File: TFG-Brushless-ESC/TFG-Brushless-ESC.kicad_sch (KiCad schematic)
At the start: 70 parts, among them J1 V, J2 USB C Receptacle, J3 HALL SENSORS, J4 SWD-I2C, J6 U, J7 W, J8 24V IN, SW1 BOOT0, SW2 NRST, U1 LM317L_SOT-89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

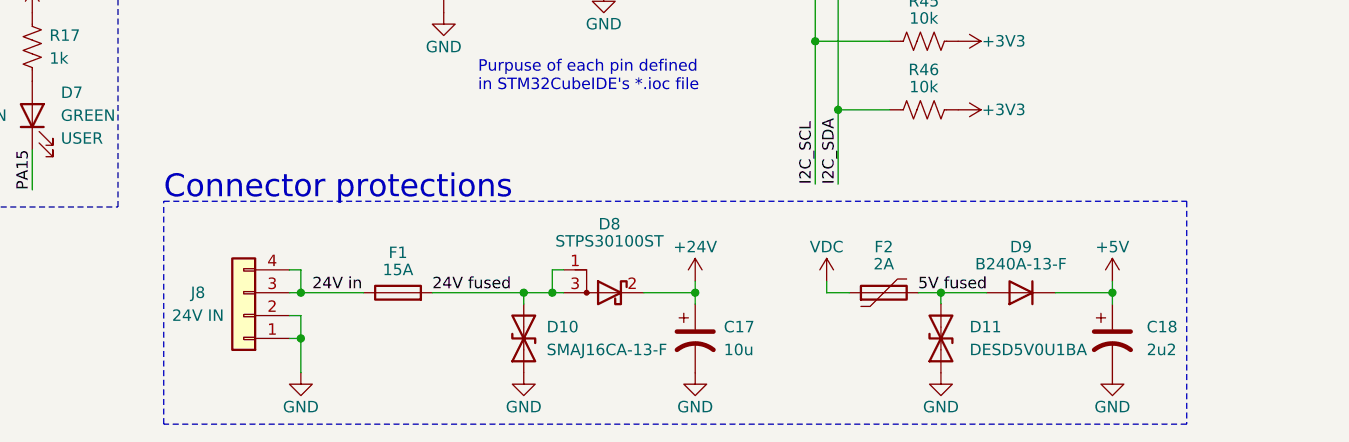
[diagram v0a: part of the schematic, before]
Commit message: renaming images
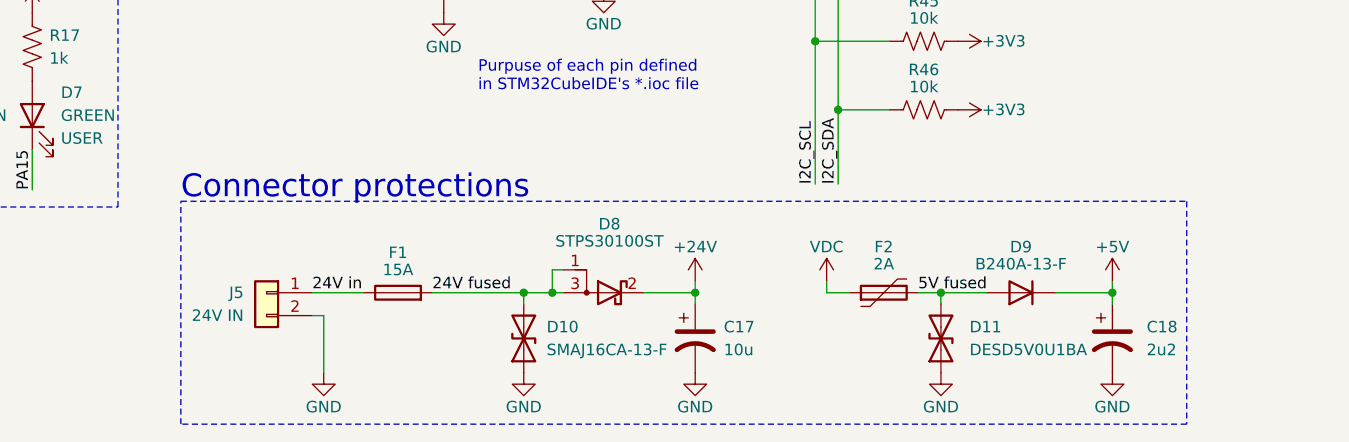
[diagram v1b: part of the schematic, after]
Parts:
- removed J8: 24V IN, Connector_Phoenix_MSTB:PhoenixContact_MSTBA_2,5_4-G-5,08_1x04_P5.08mm_Horizontal, symbol Connector_Generic:Conn_01x04
- added J5: 24V IN, Connector_Phoenix_MSTB:PhoenixContact_MSTBA_2,5_2-G-5,08_1x02_P5.08mm_Horizontal, symbol Connector_Generic:Conn_01x02
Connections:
- net 24V in: now also J5.1 (Pin_1)
- net GND: now also J5.2 (Pin_2)
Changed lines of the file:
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@@
 	)
 	(junction
-		(at 60.325 181.61)
-		(diameter 0)
-		(color 0 0 0 0)
-	)
-	(junction
 		(at 62.865 26.035)
 		(diameter 0)
@@
 	)
 	(junction
-		(at 60.325 186.69)
-		(diameter 0)
-		(color 0 0 0 0)
-	)
-	(junction
 		(at 34.29 122.555)
 		(diameter 0)
@@
 	(wire
 		(pts
-			(xy 60.325 186.69) (xy 60.325 190.5)
+			(xy 62.865 184.15) (xy 62.865 190.5)
 		)
 		(stroke
@@
 	(wire
 		(pts
-			(xy 59.055 184.15) (xy 60.325 184.15)
+			(xy 61.595 184.15) (xy 62.865 184.15)
 		)
 		(stroke
@@
 	(wire
 		(pts
-			(xy 60.325 186.69) (xy 60.325 184.15)
-		)
-		(stroke
-			(width 0)
-			(type default)
-		)
-	)
-	(wire
-		(pts
 			(xy 232.41 130.81) (xy 237.49 130.81)
 		)
@@
 	(wire
 		(pts
-			(xy 59.055 181.61) (xy 60.325 181.61)
+			(xy 61.595 181.61) (xy 67.31 181.61)
 		)
 		(stroke
@@
 	(wire
 		(pts
-			(xy 60.325 179.07) (xy 60.325 181.61)
-		)
-		(stroke
-			(width 0)
-			(type default)
-		)
-	)
-	(wire
-		(pts
 			(xy 237.49 130.81) (xy 237.49 136.525)
 		)
@@
 	(wire
 		(pts
-			(xy 59.055 186.69) (xy 60.325 186.69)
-		)
-		(stroke
-			(width 0)
-			(type default)
-		)
-	)
-	(wire
-		(pts
 			(xy 95.25 26.035) (xy 95.25 27.305)
 		)
@@
 	(wire
 		(pts
-			(xy 60.325 181.61) (xy 67.31 181.61)
-		)
-		(stroke
-			(width 0)
-			(type default)
-		)
-	)
-	(wire
-		(pts
 			(xy 164.465 36.195) (xy 164.465 33.655)
 		)
@@
 	(wire
 		(pts
-			(xy 59.055 179.07) (xy 60.325 179.07)
-		)
-		(stroke
-			(width 0)
-			(type default)
-		)
-	)
-	(wire
-		(pts
 			(xy 236.22 34.925) (xy 236.22 36.195)
 		)
@@
 	)
 	(rectangle
-		(start 45.085 171.45)
+		(start 46.99 171.45)
 		(end 158.75 196.215)
 		(stroke
@@
 	(text "Connector protections"
 		(exclude_from_sim no)
-		(at 45.085 171.45 0)
+		(at 46.99 171.45 0)
 		(effects
 			(font
@@
 	)
 	(symbol
-		(lib_id "Connector_Generic:Conn_01x04")
-		(at 53.975 184.15 180)
-		(unit 1)
-		(exclude_from_sim no)
-		(in_bom yes)
-		(on_board yes)
-		(dnp no)
-		(property "Reference" "J8"
-			(at 48.895 181.61 0)
-			(effects
-				(font
-					(size 1.27 1.27)
-				)
-			)
-		)
-		(property "Value" "24V IN"
-			(at 48.895 184.15 0)
-			(effects
-				(font
-					(size 1.27 1.27)
-				)
-			)
-		)
-		(property "Footprint" "Connector_Phoenix_MSTB:PhoenixContact_MSTBA_2,5_4-G-5,08_1x04_P5.08mm_Horizontal"
-			(at 53.975 184.15 0)
-			(effects
-				(font
-					(size 1.27 1.27)
-				)
-				(hide yes)
-			)
-		)
-		(property "Datasheet" "https://www.lcsc.com/datasheet/lcsc_datasheet_2408130957_Ningbo-Kangnex-Elec-WJ2EDGRC-5-08-4P_C8446.pdf"
-			(at 53.975 184.15 0)
-			(effects
-				(font
-					(size 1.27 1.27)
-				)
-				(hide yes)
-			)
-		)
-		(property "Description" "C8446"
-			(at 53.975 184.15 0)
-			(effects
-				(font
-					(size 1.27 1.27)
-				)
-				(hide yes)
-			)
-		)
-		(pin "1"
-		)
-		(pin "3"
-		)
-		(pin "2"
-		)
-		(pin "4"
-		)
-		(instances
-			(project ""
-				(path "/fc8dd9a9-f99a-4338-8182-2c8b4b8ed6dd"
-					(reference "J8")
-					(unit 1)
-				)
-			)
-		)
-	)
-	(symbol
 		(lib_id "Device:R_US")
 		(at 95.25 31.115 0)
@@
 	(symbol
 		(lib_id "power:GND")
-		(at 60.325 190.5 0)
+		(at 62.865 190.5 0)
 		(mirror y)
 		(unit 1)
@@
 		(dnp no)
 		(property "Reference" "#PWR054"
-			(at 60.325 196.85 0)
+			(at 62.865 196.85 0)
 			(effects
 				(font
@@
 		)
 		(property "Value" "GND"
-			(at 60.325 194.31 0)
+			(at 62.865 194.31 0)
 			(effects
 				(font
@@
 		)
 		(property "Footprint" ""
-			(at 60.325 190.5 0)
+			(at 62.865 190.5 0)
 			(effects
 				(font
@@
 		)
 		(property "Datasheet" ""
-			(at 60.325 190.5 0)
+			(at 62.865 190.5 0)
 			(effects
 				(font
@@
 		)
 		(property "Description" ""
-			(at 60.325 190.5 0)
+			(at 62.865 190.5 0)
 			(effects
 				(font
@@
 					(unit 1)
 				)
+			)
+		)
+	)
+	(symbol
+		(lib_id "Connector_Generic:Conn_01x02")
+		(at 56.515 181.61 0)
+		(mirror y)
+		(unit 1)
+		(exclude_from_sim no)
+		(in_bom yes)
+		(on_board yes)
+		(dnp no)
+		(property "Reference" "J5"
+			(at 53.975 181.61 0)
+			(effects
+				(font
+					(size 1.27 1.27)
+				)
+				(justify left)
+			)
+		)
+		(property "Value" "24V IN"
+			(at 53.975 184.15 0)
+			(effects
+				(font
+					(size 1.27 1.27)
+				)
+				(justify left)
+			)
+		)
+		(property "Footprint" "Connector_Phoenix_MSTB:PhoenixContact_MSTBA_2,5_2-G-5,08_1x02_P5.08mm_Horizontal"
+			(at 56.515 181.61 0)
+			(effects
+				(font
+					(size 1.27 1.27)
+				)
+				(hide yes)
+			)
+		)
+		(property "Datasheet" "https://www.lcsc.com/datasheet/lcsc_datasheet_2408130957_Ningbo-Kangnex-Elec-WJ2EDGRC-5-08-2P_C3697.pdf"
+			(at 56.515 181.61 0)
+			(effects
+				(font
+					(size 1.27 1.27)
+				)
+				(hide yes)
+			)
+		)
+		(property "Description" "C3697"
+			(at 56.515 181.61 0)
+			(effects
+				(font
+					(size 1.27 1.27)
+				)
+				(hide yes)
+			)
+		)
+		(pin "2"
+		)
+		(pin "1"
+		)
+		(instances
+			(project "TFG-Brushless-ESC"
+				(path "/fc8dd9a9-f99a-4338-8182-2c8b4b8ed6dd"
+					(reference "J5")
+					(unit 1)
+				)

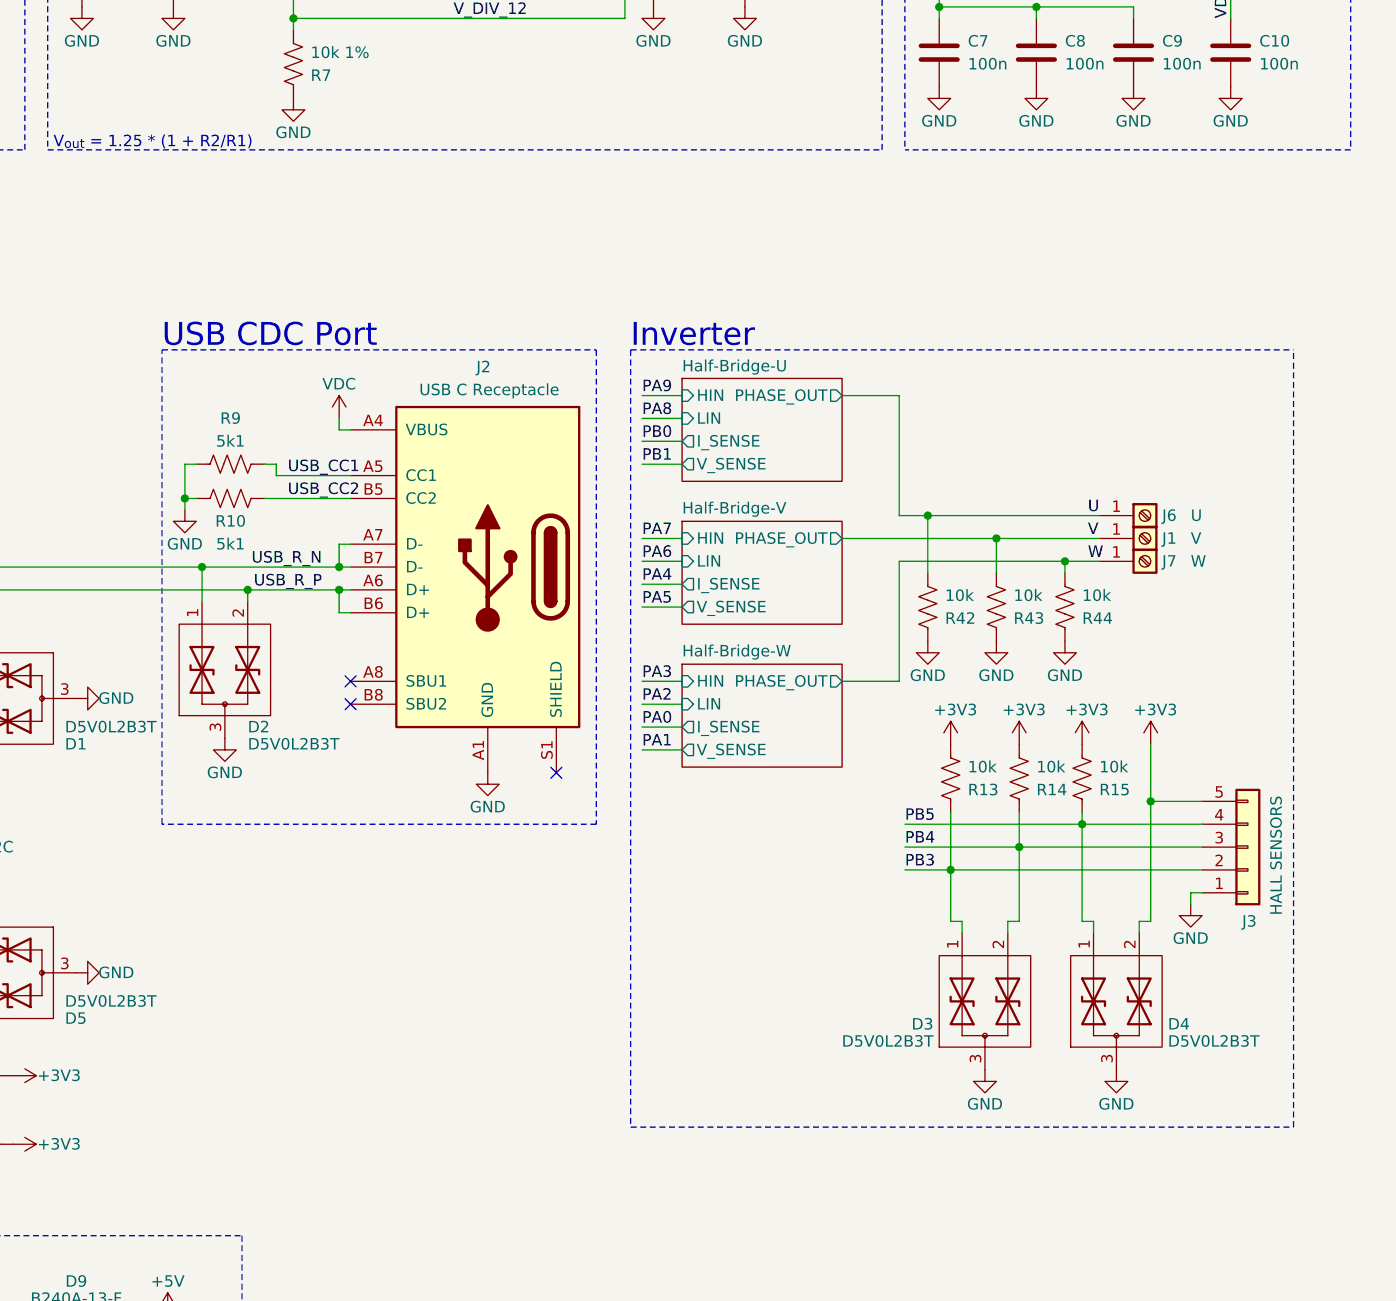
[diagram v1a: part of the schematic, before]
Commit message: Added fan control and temp measurement. Not added to pcb yet
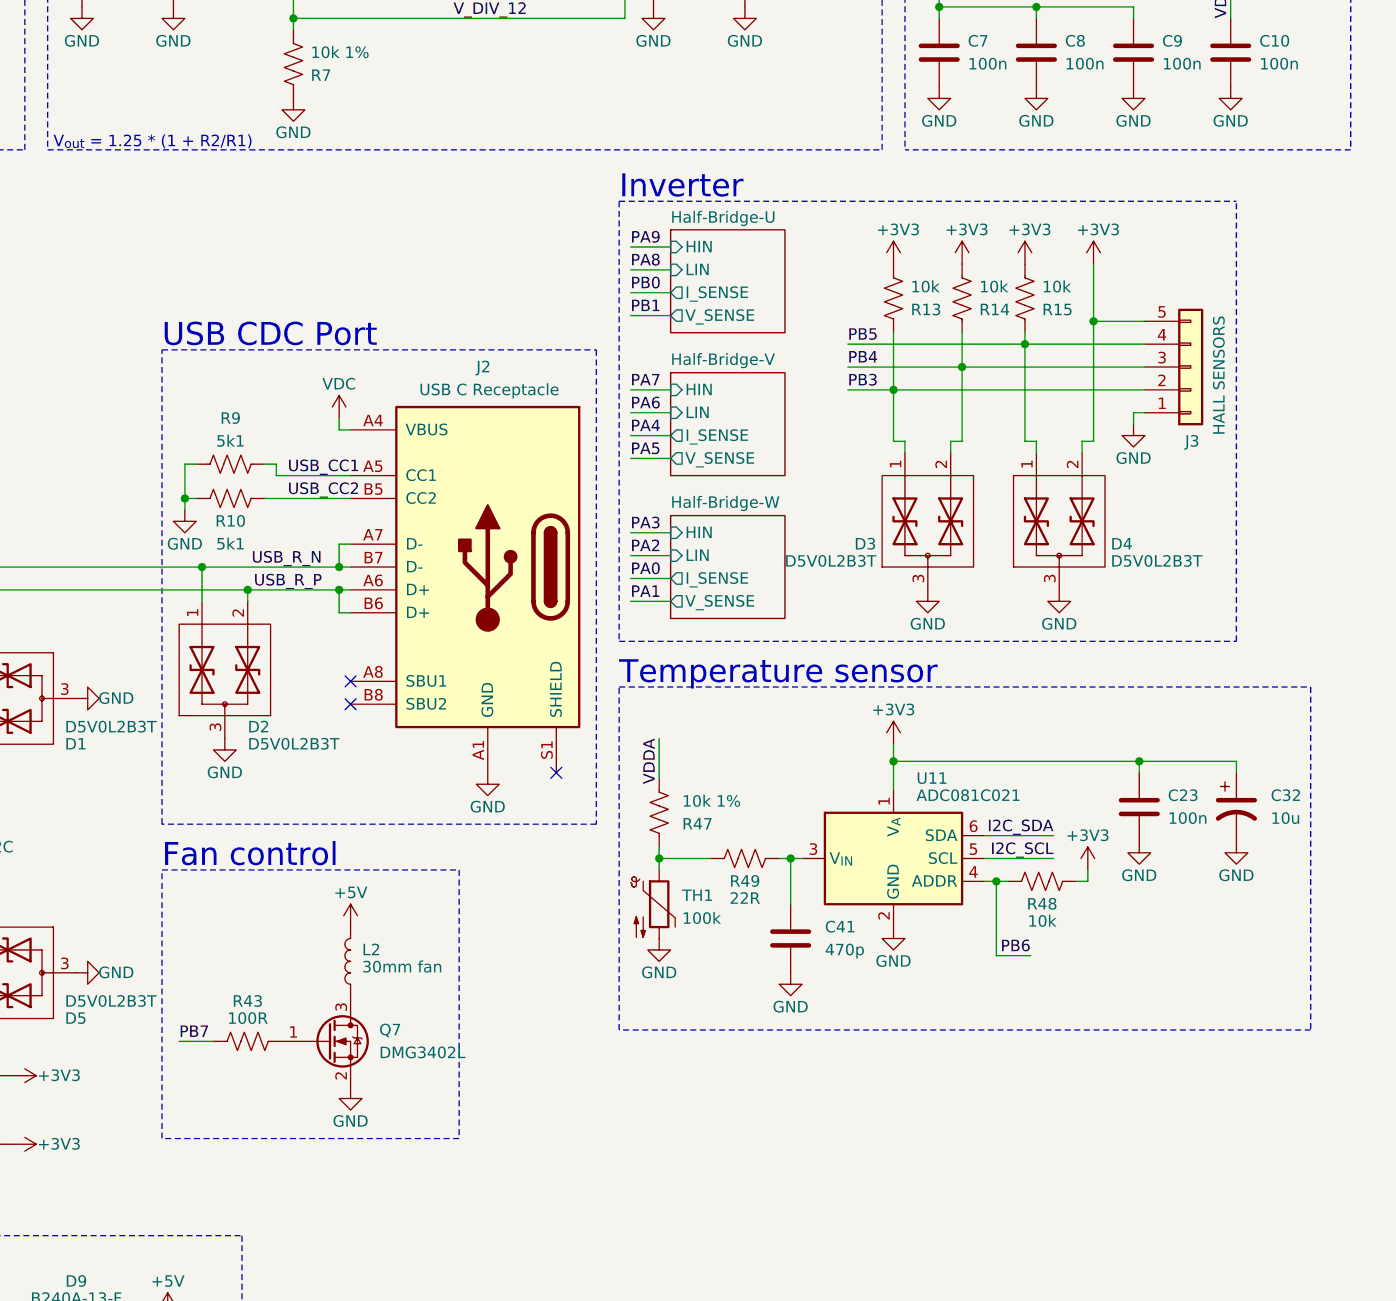
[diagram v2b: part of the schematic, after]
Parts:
- removed J1: V, TFG-Brushless-ESC:Screw_Terminal, symbol Connector:Screw_Terminal_01x01
- removed J6: U, TFG-Brushless-ESC:Screw_Terminal, symbol Connector:Screw_Terminal_01x01
- removed J7: W, TFG-Brushless-ESC:Screw_Terminal, symbol Connector:Screw_Terminal_01x01
- removed R42, R44: 10k, Resistor_SMD:R_0603_1608Metric, symbol Device:R_US
- added C23: 100n, Capacitor_SMD:C_0603_1608Metric, symbol Device:C
- added C32: 10u, Capacitor_SMD:CP_Elec_4x5.4, symbol Device:C_Polarized_US
- added C41: 470p, symbol Device:C
- added L2: 30mm fan, Connector_PinHeader_1.00mm:PinHeader_1x02_P1.00mm_Vertical, symbol Device:L
- added Q7: DMG3402L, Package_TO_SOT_SMD:SOT-23, symbol Transistor_FET:DMG3402L
- added R47: 10k 1%, Resistor_SMD:R_0603_1608Metric, symbol Device:R_US
- added R48: 10k, Resistor_SMD:R_0603_1608Metric, symbol Device:R_US
- added R49: 22R, Resistor_SMD:R_0603_1608Metric, symbol Device:R_US
- added TH1: 100k, Connector_PinHeader_1.00mm:PinHeader_1x02_P1.00mm_Vertical, symbol Device:Thermistor_NTC
- added U11: ADC081C021, Package_TO_SOT_SMD:SOT-23-6, symbol Analog_ADC:ADC101C021CIMK
- R43: value 10k -> 100R; footprint Resistor_SMD:R_0603_1608Metric -> Resistor_SMD:R_0805_2012Metric
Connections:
- net +3V3: now also C23.1, C32.1, R48.1, U11.1 (V_{A})
- net +5V: now also L2.2
- net GND: now also C23.2, C32.2, C41.2, Q7.2 (S), TH1.2, U11.2 (GND); no longer R43.1
- net I2C_SCL: now also U11.5 (SCL)
- net I2C_SDA: now also U11.6 (SDA)
- net PB6: now also R48.2, U11.4 (ADDR)
- net PB7: now also R43.1
- net VDDA: now also R47.2
- net V: no longer names the net of R43.2
- net V: now also Q7.1 (G)
- new net: C41.1, R49.1, U11.3 (V_{IN})
- new net: R47.1, R49.2, TH1.1
- new net: L2.1, Q7.3 (D)
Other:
- sheet Half-Bridge-U ports: added none; removed PHASE_OUT
- sheet Half-Bridge-V ports: added none; removed PHASE_OUT
- sheet Half-Bridge-W ports: added none; removed PHASE_OUT
- note added: "Fan control"
- note added: "Temperature sensor"
- moved on the sheet: D3, D4, J3, R13, R14, R15
